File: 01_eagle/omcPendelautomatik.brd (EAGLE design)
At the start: 44.5 x 69.8 mm, 71 parts, among them IC1 PIC12F675, IC2 7805, IC3 L5970D, K1 NA-5V, T1 BSS138, T2 BSS138, X1 RT034 Typ 086, X2 2X3

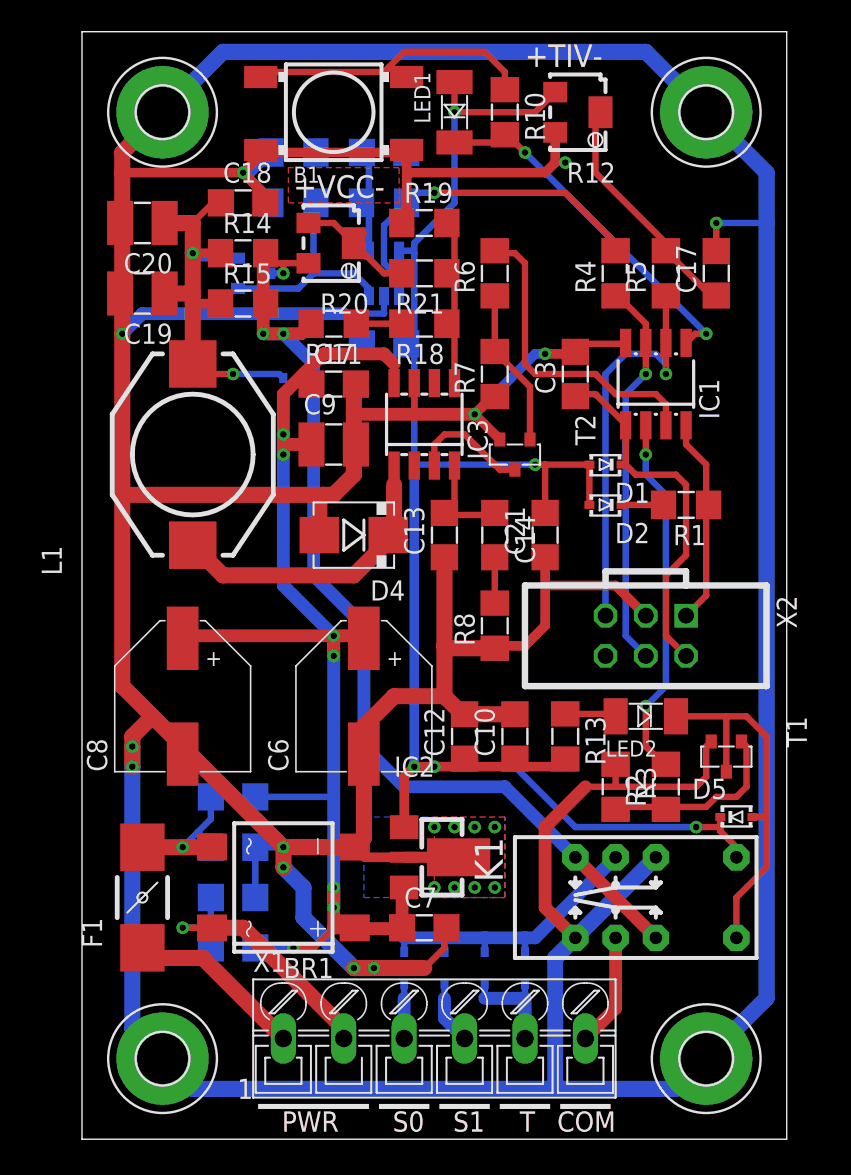
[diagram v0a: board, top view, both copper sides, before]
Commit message: omcPendelautomatik.brd -> adjust silk print on top side
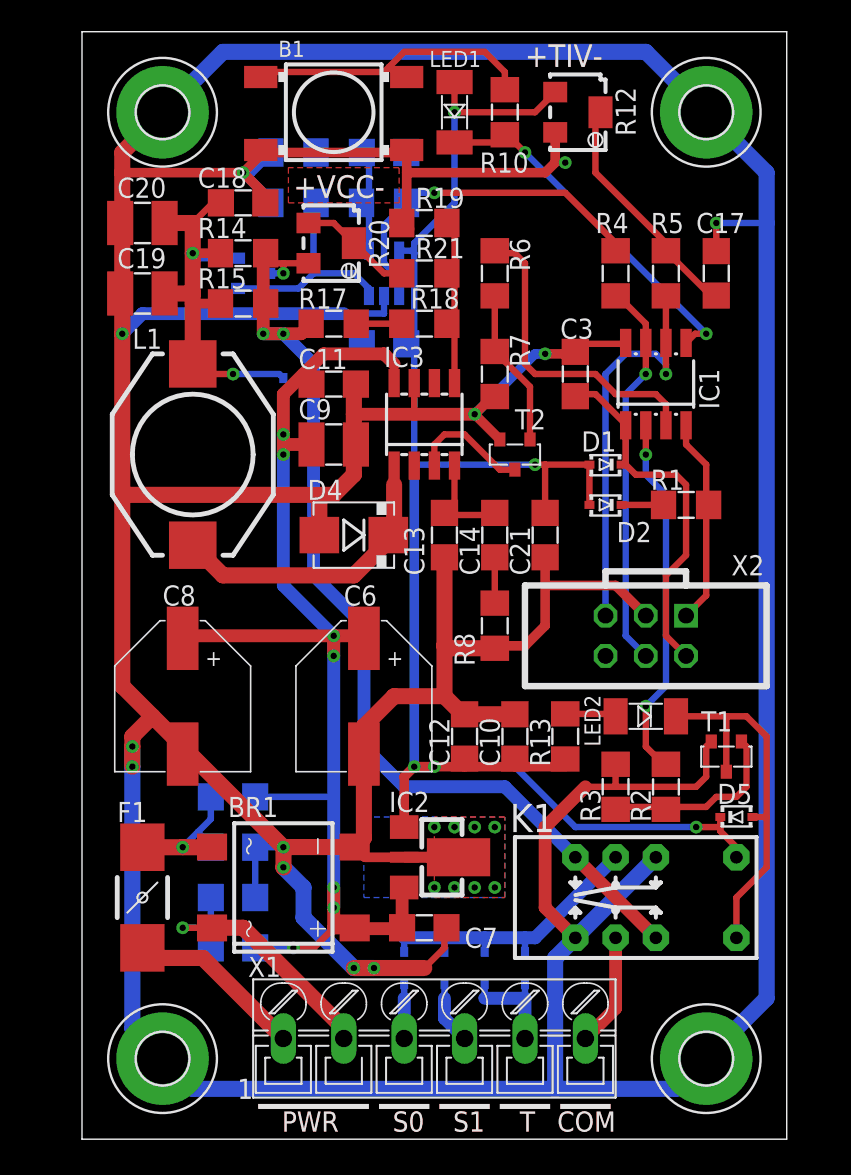
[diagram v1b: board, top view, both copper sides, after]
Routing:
- net N$2: track 8.09 -> 7.20 mm
